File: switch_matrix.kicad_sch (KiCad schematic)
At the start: 0 parts

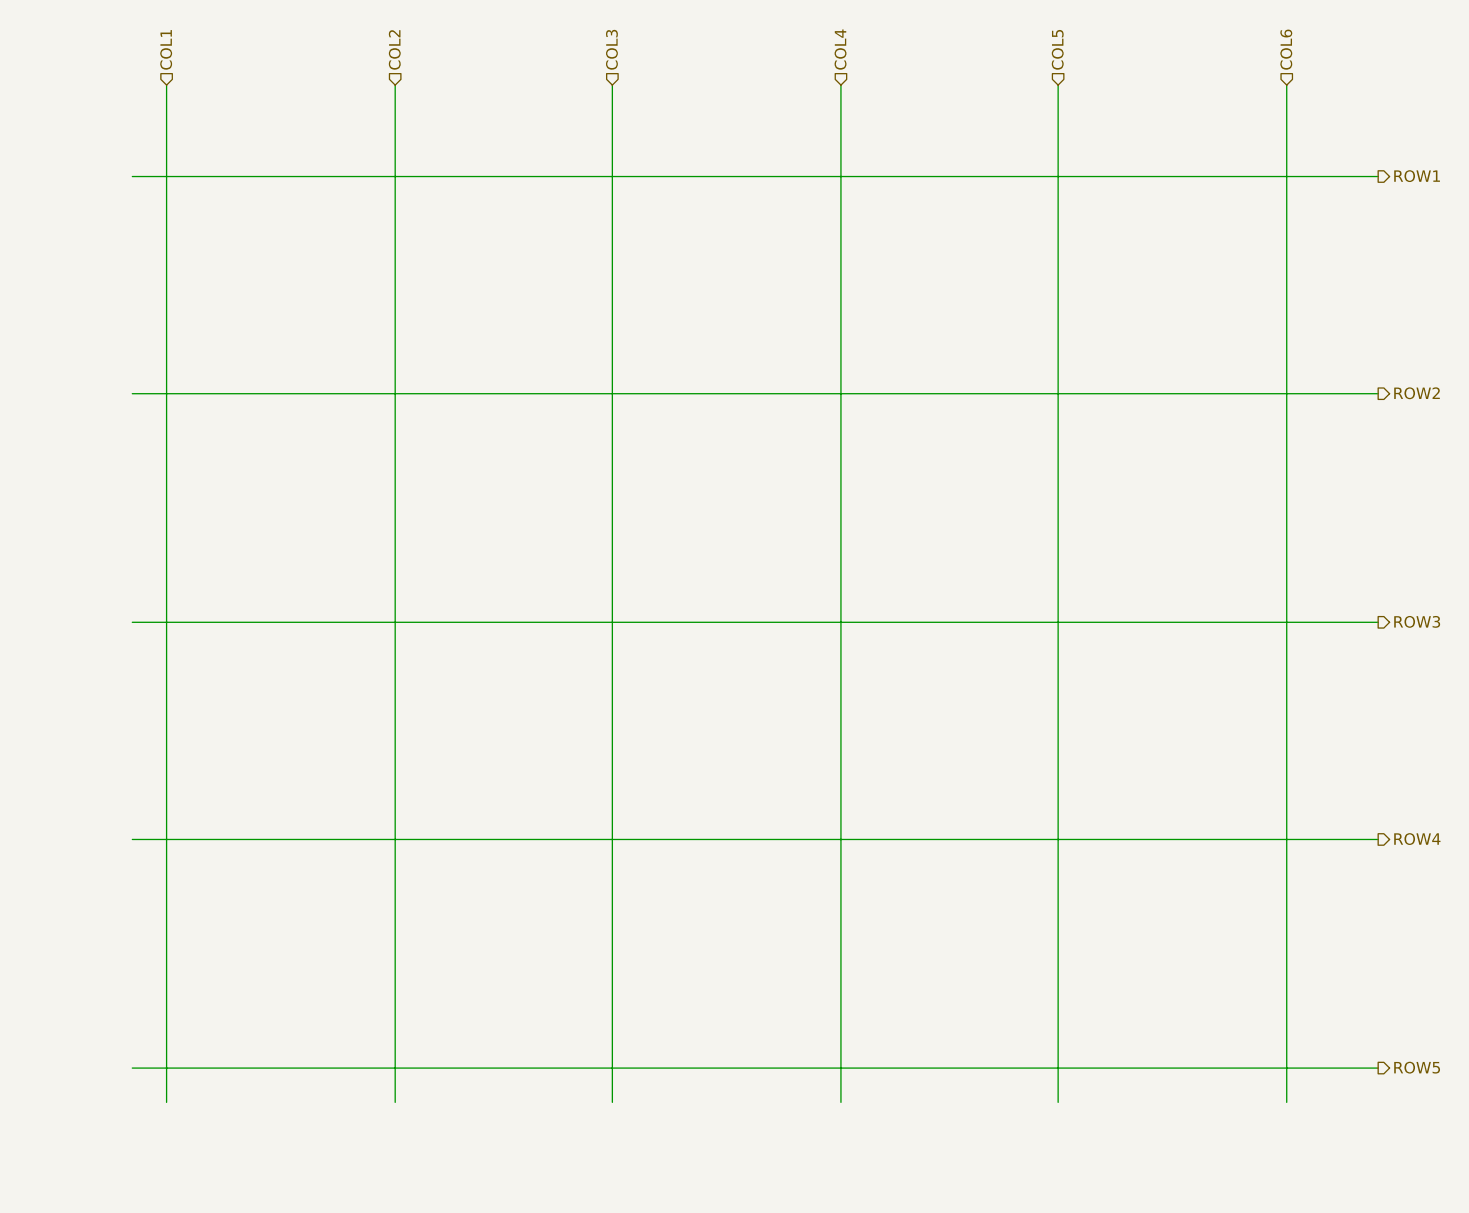
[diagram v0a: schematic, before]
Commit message: added switch matrix
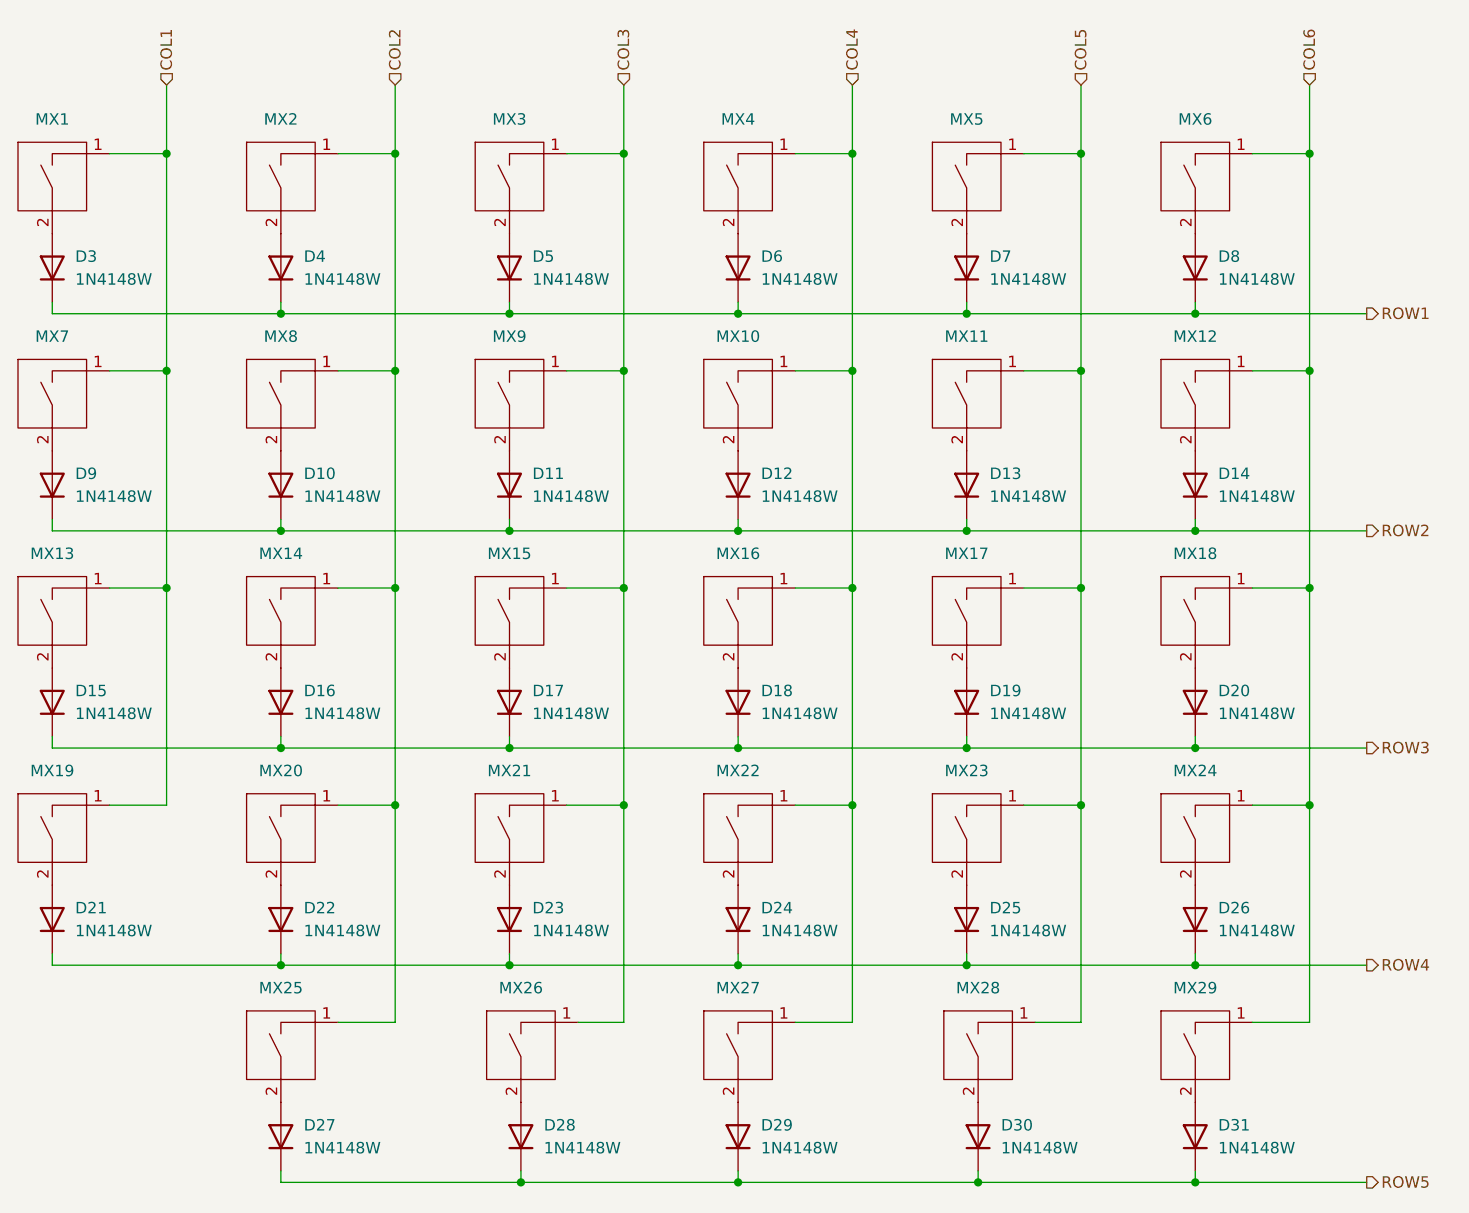
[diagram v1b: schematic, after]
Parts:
- added D10, D11, D12, D13, D14, D15, D16, D17, D18, D19, D20, D21, D22, D23, D24, D25, D26, D27, D28, D29, D3, D30, D31, D4, D5, D6, D7, D8, D9: 1N4148W, Diode_SMD:D_SOD-123, symbol Diode:1N4148W
- added MX1, MX10, MX11, MX12, MX13, MX14, MX15, MX16, MX17, MX18, MX19, MX2, MX20, MX21, MX22, MX23, MX24, MX25, MX26, MX27, MX28, MX29, MX3, MX4, MX5, MX6, MX7, MX8, MX9: ~, symbol Lily58:Cherry_MX2A
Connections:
- net COL1: now also MX1.1, MX13.1, MX19.1, MX7.1
- net COL2: now also MX14.1, MX2.1, MX20.1, MX25.1, MX8.1
- net COL3: now also MX15.1, MX21.1, MX26.1, MX3.1, MX9.1
- net COL4: now also MX10.1, MX16.1, MX22.1, MX27.1, MX4.1
- net COL5: now also MX11.1, MX17.1, MX23.1, MX28.1, MX5.1
- net COL6: now also MX12.1, MX18.1, MX24.1, MX29.1, MX6.1
- net ROW1: now also D3.1 (K), D4.1 (K), D5.1 (K), D6.1 (K), D7.1 (K), D8.1 (K)
- net ROW2: now also D10.1 (K), D11.1 (K), D12.1 (K), D13.1 (K), D14.1 (K), D9.1 (K)
- net ROW3: now also D15.1 (K), D16.1 (K), D17.1 (K), D18.1 (K), D19.1 (K), D20.1 (K)
- net ROW4: now also D21.1 (K), D22.1 (K), D23.1 (K), D24.1 (K), D25.1 (K), D26.1 (K)
- net ROW5: now also D27.1 (K), D28.1 (K), D29.1 (K), D30.1 (K), D31.1 (K)
- new net: D17.2 (A), MX15.2
- new net: D5.2 (A), MX3.2
- new net: D27.2 (A), MX25.2
- new net: D22.2 (A), MX20.2
- new net: D21.2 (A), MX19.2
- new net: D13.2 (A), MX11.2
- new net: D26.2 (A), MX24.2
- new net: D6.2 (A), MX4.2
- new net: D12.2 (A), MX10.2
- new net: D29.2 (A), MX27.2
- new net: D25.2 (A), MX23.2
- new net: D8.2 (A), MX6.2
- new net: D7.2 (A), MX5.2
- new net: D24.2 (A), MX22.2
- new net: D20.2 (A), MX18.2
- new net: D4.2 (A), MX2.2
- new net: D30.2 (A), MX28.2
- new net: D19.2 (A), MX17.2
- new net: D16.2 (A), MX14.2
- new net: D18.2 (A), MX16.2
- new net: D9.2 (A), MX7.2
- new net: D11.2 (A), MX9.2
- new net: D14.2 (A), MX12.2
- new net: D28.2 (A), MX26.2
- new net: D10.2 (A), MX8.2
- new net: D3.2 (A), MX1.2
- new net: D23.2 (A), MX21.2
- new net: D15.2 (A), MX13.2
- new net: D31.2 (A), MX29.2
